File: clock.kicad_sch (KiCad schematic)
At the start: 32 parts, among them P16 SMA, P2 SMA, U19 SI5351C, U30 74LVC1G3157, U31 74LVC1G3157, U33 74HC4051, X1 TCXO

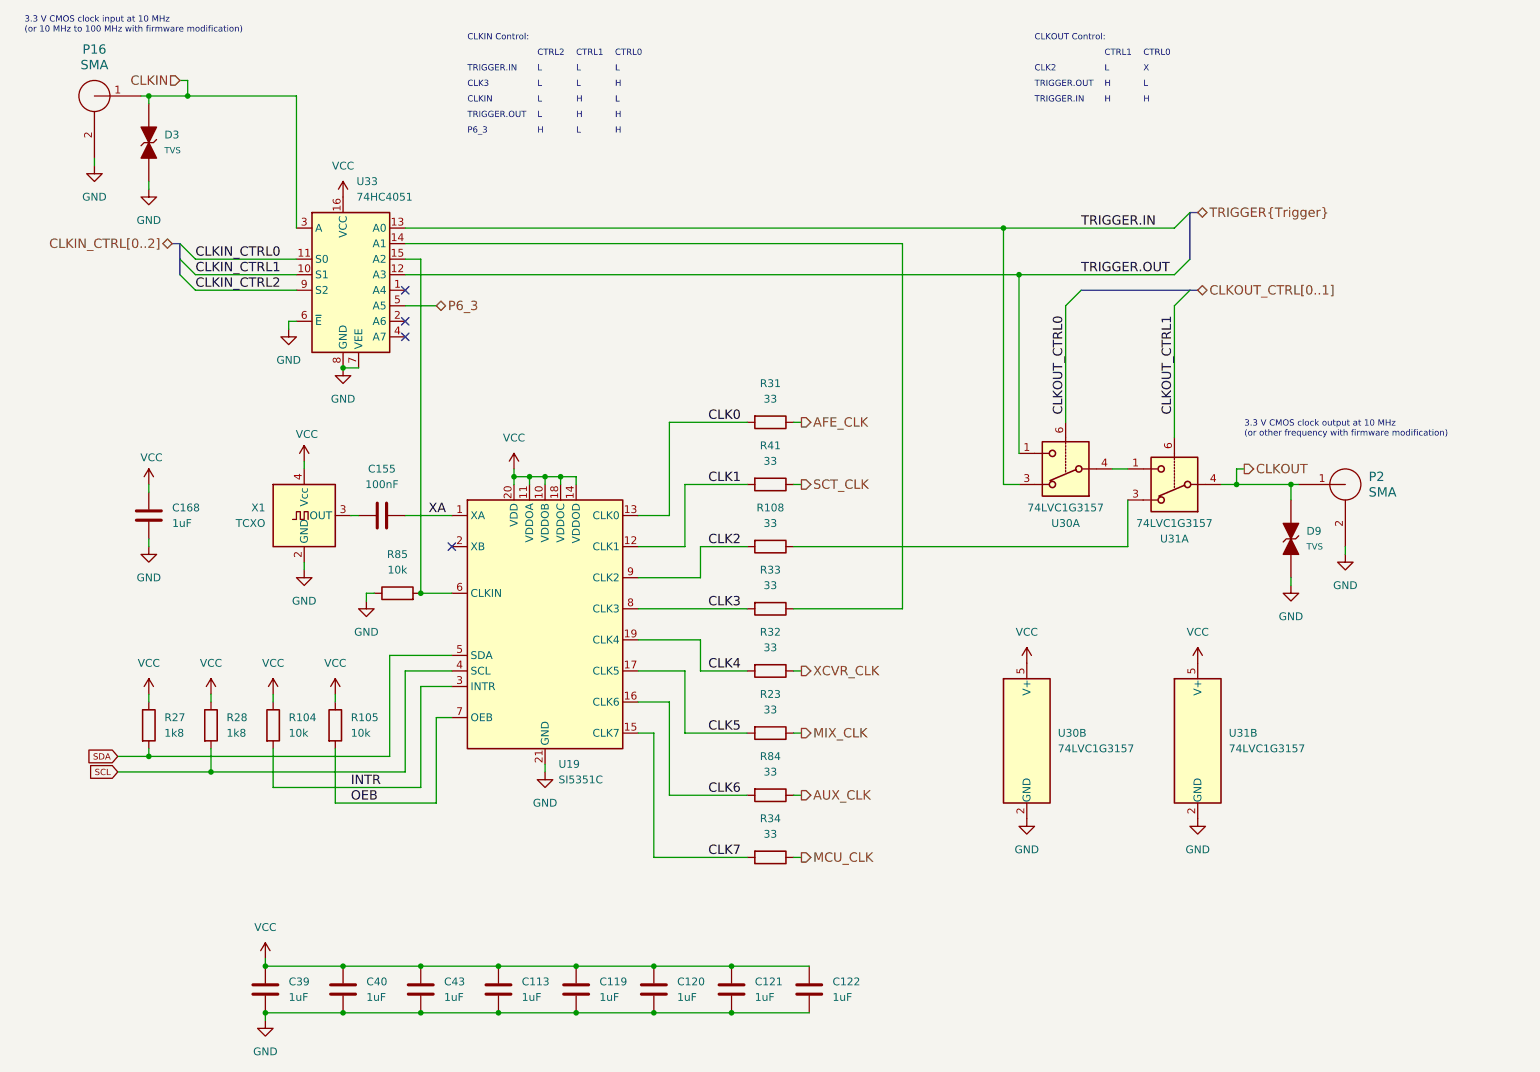
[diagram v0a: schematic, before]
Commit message: Move clock generator U19 to 3V3FPGA supply
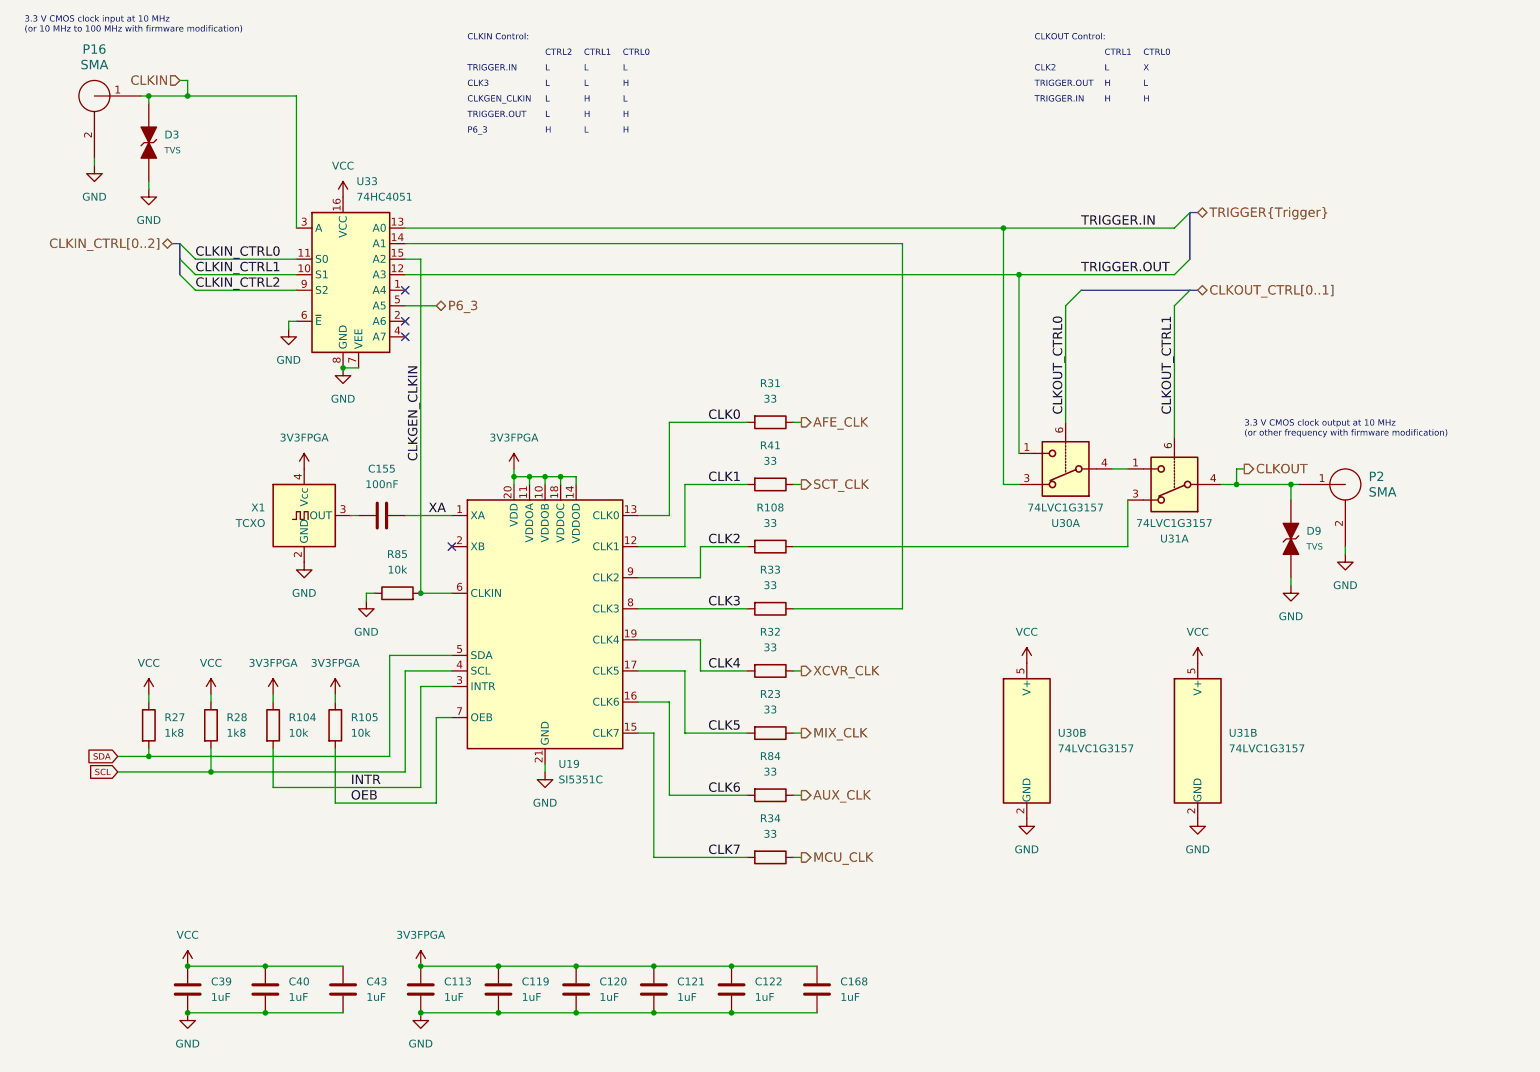
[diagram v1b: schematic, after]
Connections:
- net VCC: no longer C113.1, C119.1, C120.1, C121.1, C122.1, C168.2, R104.1, R105.1, U19.10 (VDDOB), U19.11 (VDDOA), U19.14 (VDDOD), U19.18 (VDDOC), U19.20 (VDD), X1.4 (Vcc)
- net CLKGEN_CLKIN: now reaches R85.2, U19.6 (CLKIN), U33.15 (A2)
- new net 3V3FPGA: C113.1, C119.1, C120.1, C121.1, C122.1, C168.2, R104.1, R105.1, U19.10 (VDDOB), U19.11 (VDDOA), U19.14 (VDDOD), U19.18 (VDDOC), U19.20 (VDD), X1.4 (Vcc)
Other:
- note added: "CLKGEN_CLKIN"
- note removed: "CLKIN"
- moved on the sheet: C113, C119, C120, C121, C122, C168, C39, C40, C43

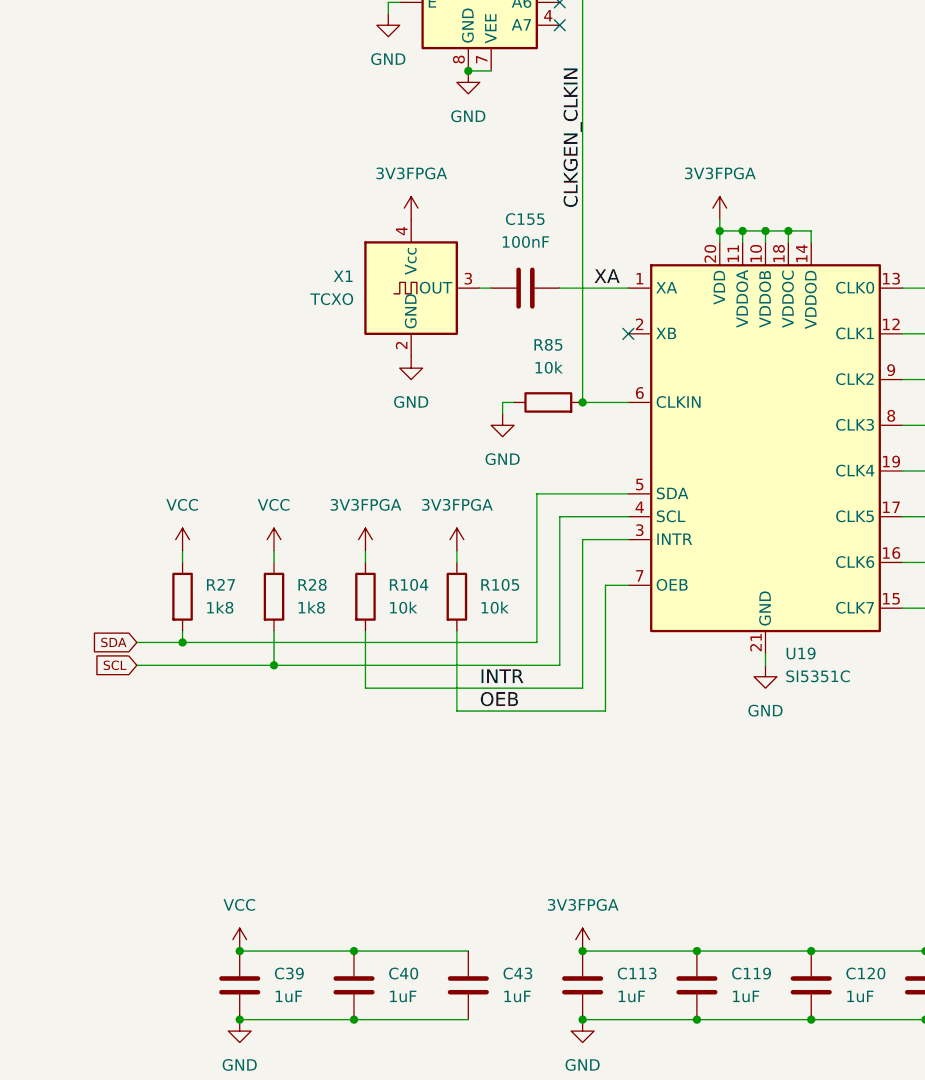
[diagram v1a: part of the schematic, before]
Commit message: Improve power supply filtering and decoupling
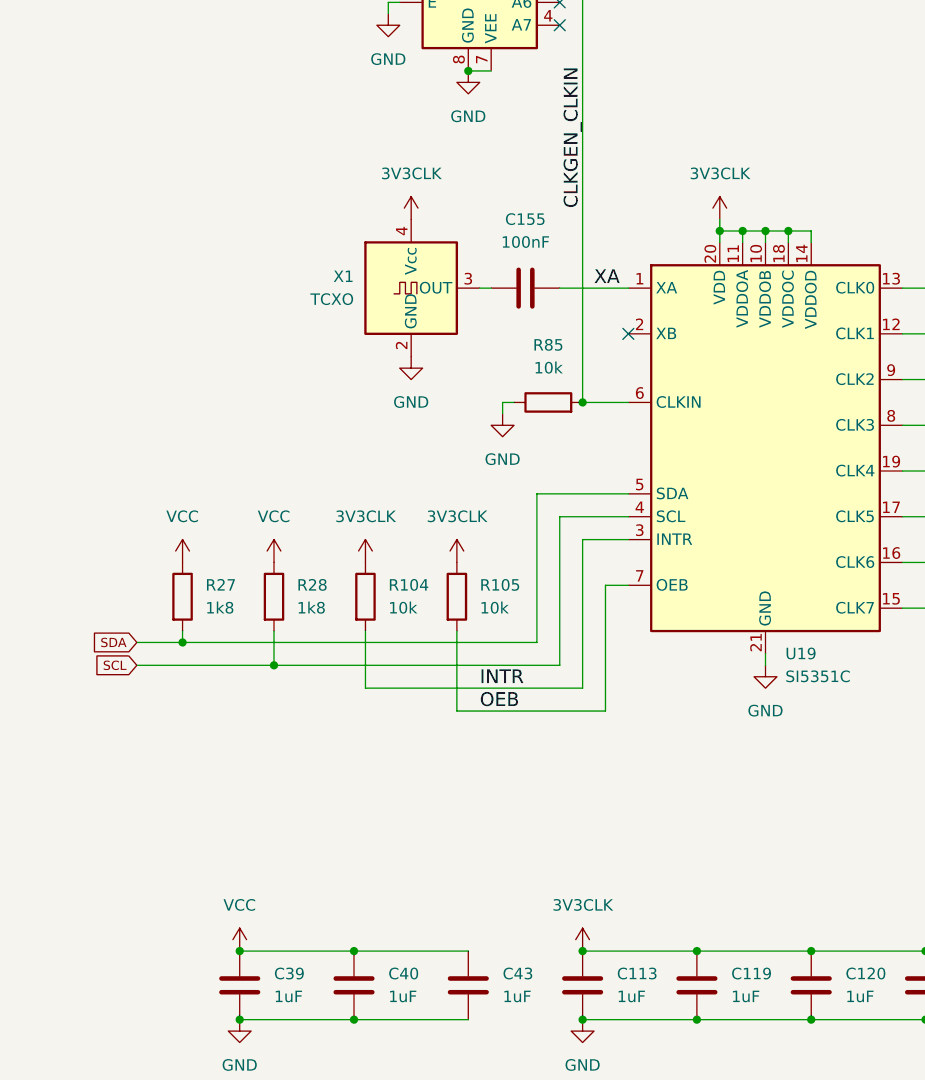
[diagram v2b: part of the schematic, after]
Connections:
- net 3V3FPGA renamed 3V3CLK

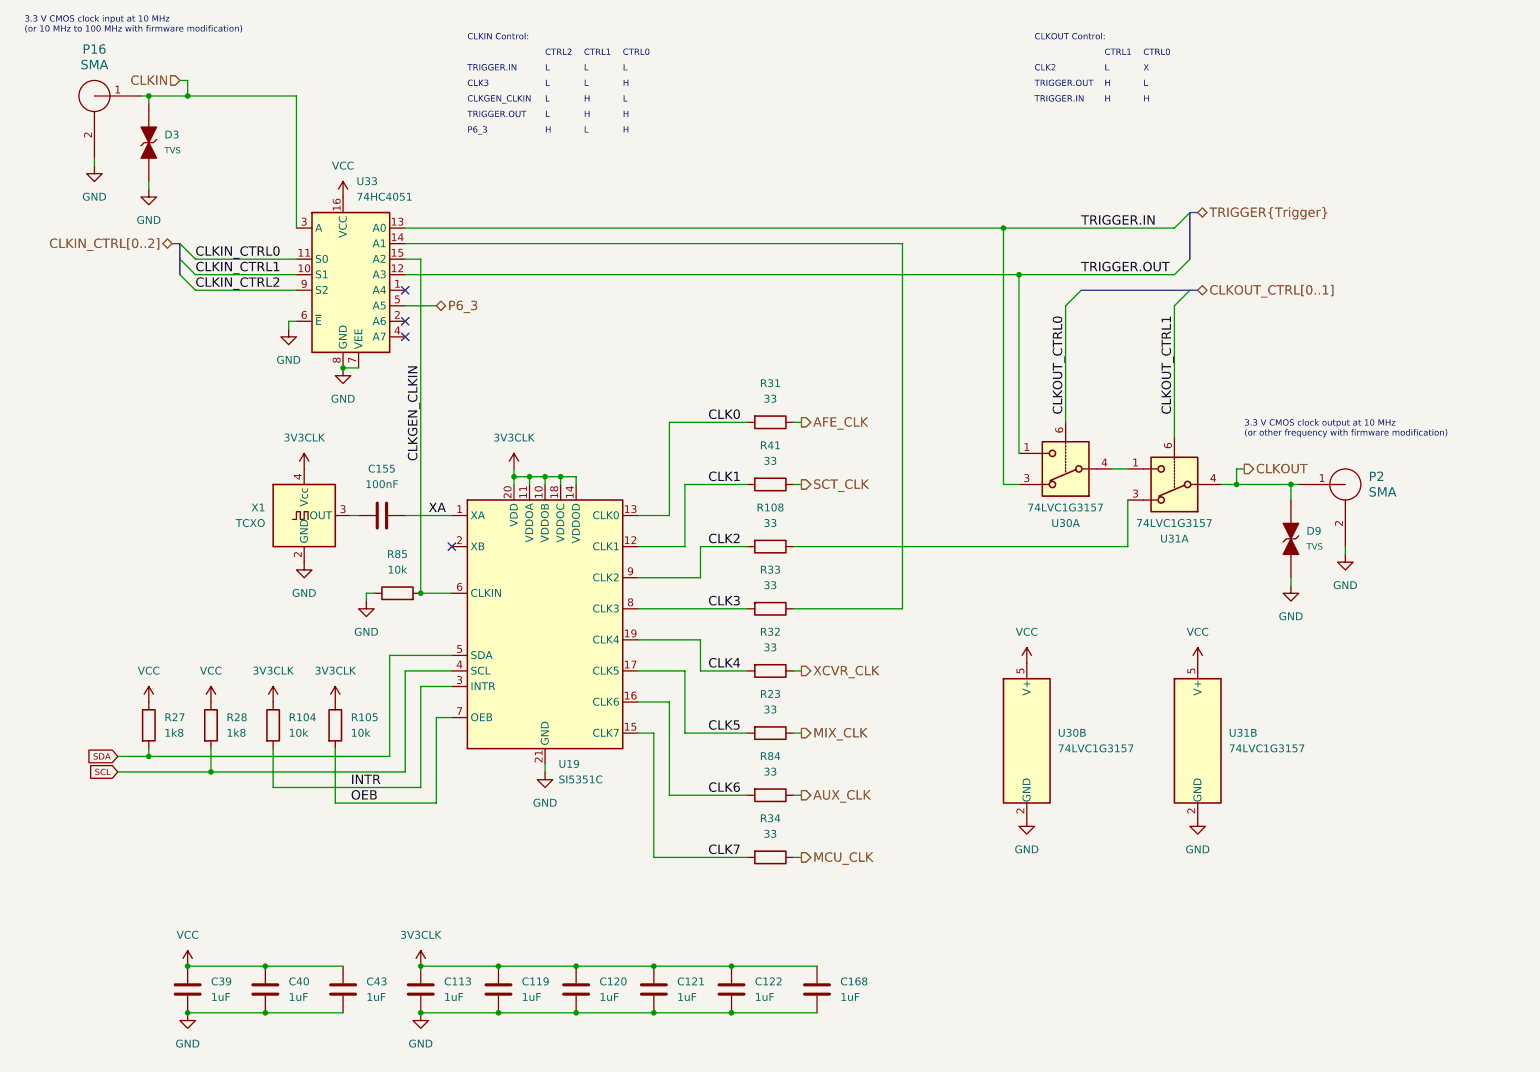
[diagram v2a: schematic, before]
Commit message: Update TVS
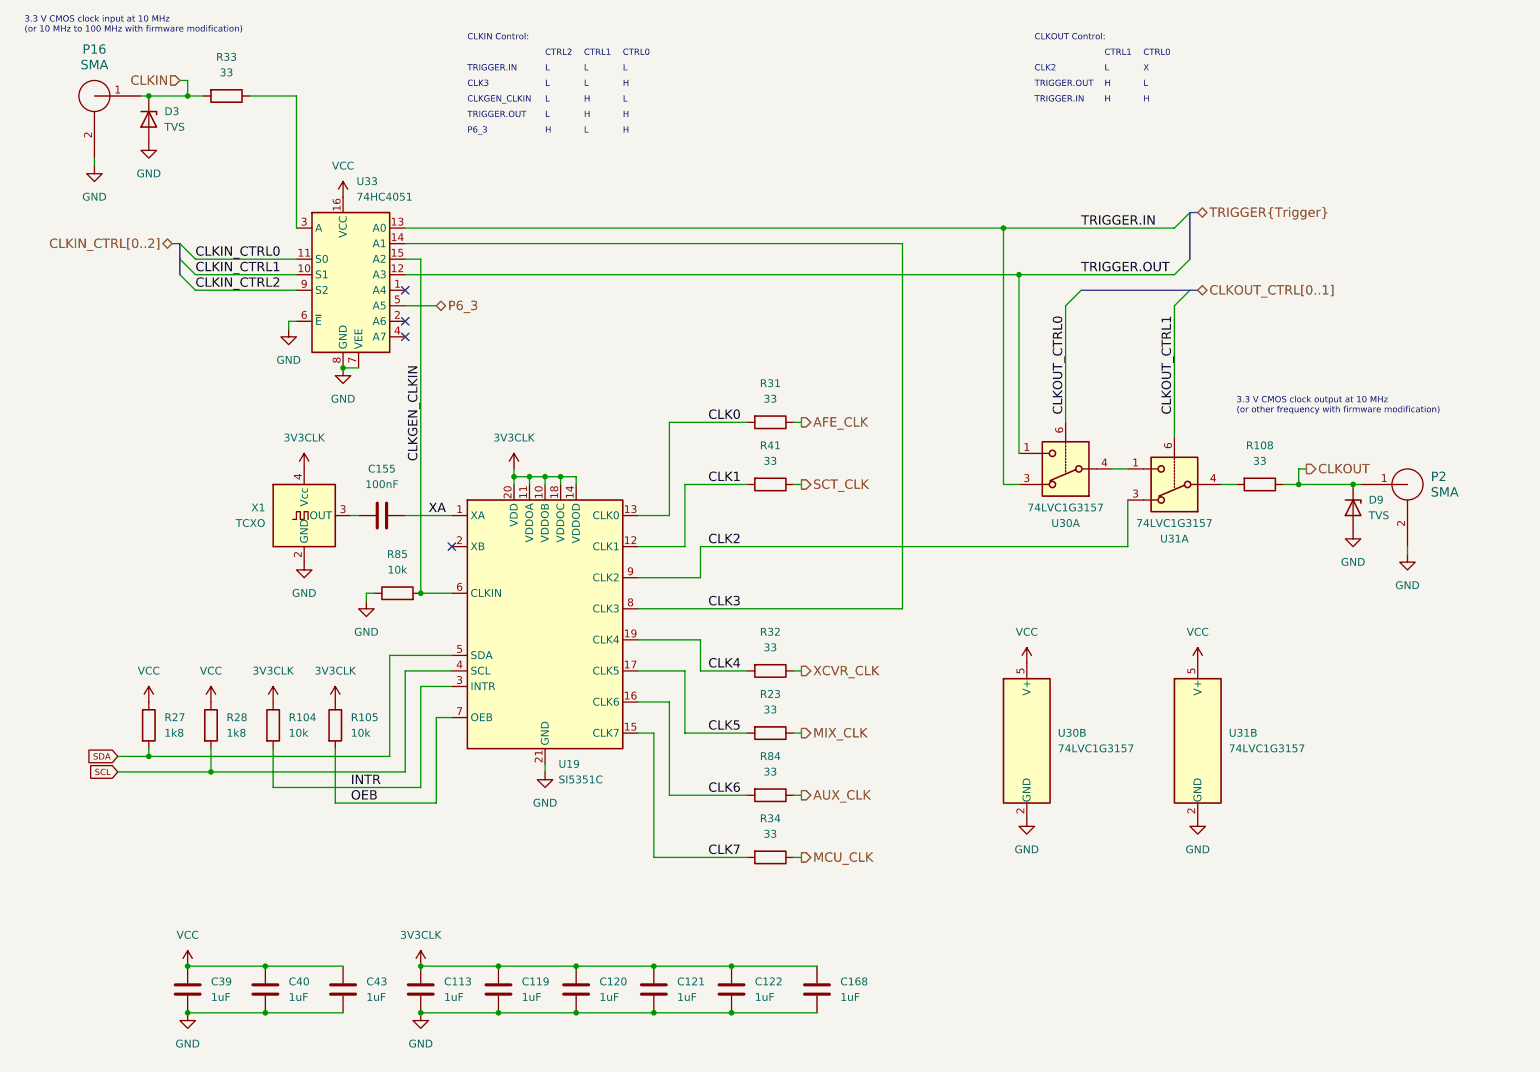
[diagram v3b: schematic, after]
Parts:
- removed D3, D9: TVS, hackrf:GSG-0402, symbol hackrf:GSG-DIODE-TVS-BI
- added D3, D9: TVS, praline:DFN1006-2, symbol Device:D_Zener
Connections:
- net CLK2: now also U31.3; no longer R108.2
- net CLK3: now also U33.14 (A1); no longer R33.2
- net CLKIN: now also R33.2, D3.1 (K); no longer U33.3 (A)
- net CLKOUT: now also R108.1, D9.1 (K); no longer U31.4
- net GND: now also D3.2 (A), D9.2 (A)
- net at R33.1: now also U33.3 (A); no longer U33.14 (A1)
- new net: R108.2, U31.4
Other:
- moved on the sheet: P2, R108, R33

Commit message: Update symbols and footprints
- Update U21 symbol and footprint
- Add L10, L11 3D model
- Add T1, T2 3D model
- Update U29 footprint
- Update J10 footprint and part selection, change to TP6
- Update diode footprints and 3D models
- Update SMA connector footprint
- Fix 3D model scale for various footprints
- Change L1 from 0603 back to 0201
- Fix pin header 3D models
- Add component substitutions
- Update RF switch and amplifier footprints
- Remove fiducials
- Update mounting hole symbol and footprint
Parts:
- P16, P2: Substitution (none) -> M04-0102170R0A
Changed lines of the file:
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@@
+			)
+		)
+		(property "Substitution" "M04-0102170R0A"
+			(at 41.91 35.56 0)
+			(effects
+				(font
+					(size 1.27 1.27)
+				)
+				(hide yes)
 			)
 		)
@@
 				)
 				(hide yes)
+			)
+		)
+		(property "Substitution" "M04-0102170R0A"
+			(at 256.54 99.06 0)
+			(effects
+				(font
+					(size 1.27 1.27)
+				)
+				(hide yes)
